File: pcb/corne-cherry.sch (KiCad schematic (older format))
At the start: 142 parts, among them J1 MJ-4PP-9, J2 OLED, J3 MJ-4PP-9, J4 OLED, J5 Conn_01x01_Male, J6 Conn_01x01_Male, P1 Conn_01x03, P3 Conn_01x03, SW1 SW_PUSH, SW10 SW_PUSH, SW11 SW_PUSH, SW12 SW_PUSH, SW13 SW_PUSH, SW14 SW_PUSH, SW15 SW_PUSH, SW16 SW_PUSH, SW17 SW_PUSH, SW18 SW_PUSH, SW19 SW_PUSH, SW2 SW_PUSH, SW20 SW_PUSH, SW21 SW_PUSH, SW22 SW_PUSH, SW23 SW_PUSH, SW24 SW_PUSH, SW25 SW_PUSH, SW26 SW_PUSH, SW27 SW_PUSH, SW28 SW_PUSH, SW29 SW_PUSH, SW3 SW_PUSH, SW30 SW_PUSH, SW31 SW_PUSH, SW32 SW_PUSH, SW33 SW_PUSH, SW34 SW_PUSH, SW35 SW_PUSH, SW36 SW_PUSH, SW37 SW_PUSH, SW38 SW_PUSH, SW39 SW_PUSH, SW4 SW_PUSH, SW40 SW_PUSH, SW41 SW_PUSH, SW42 SW_PUSH, SW5 SW_PUSH, SW6 SW_PUSH, SW7 SW_PUSH, SW8 SW_PUSH, SW9 SW_PUSH, U1 ProMicro, U2 ProMicro

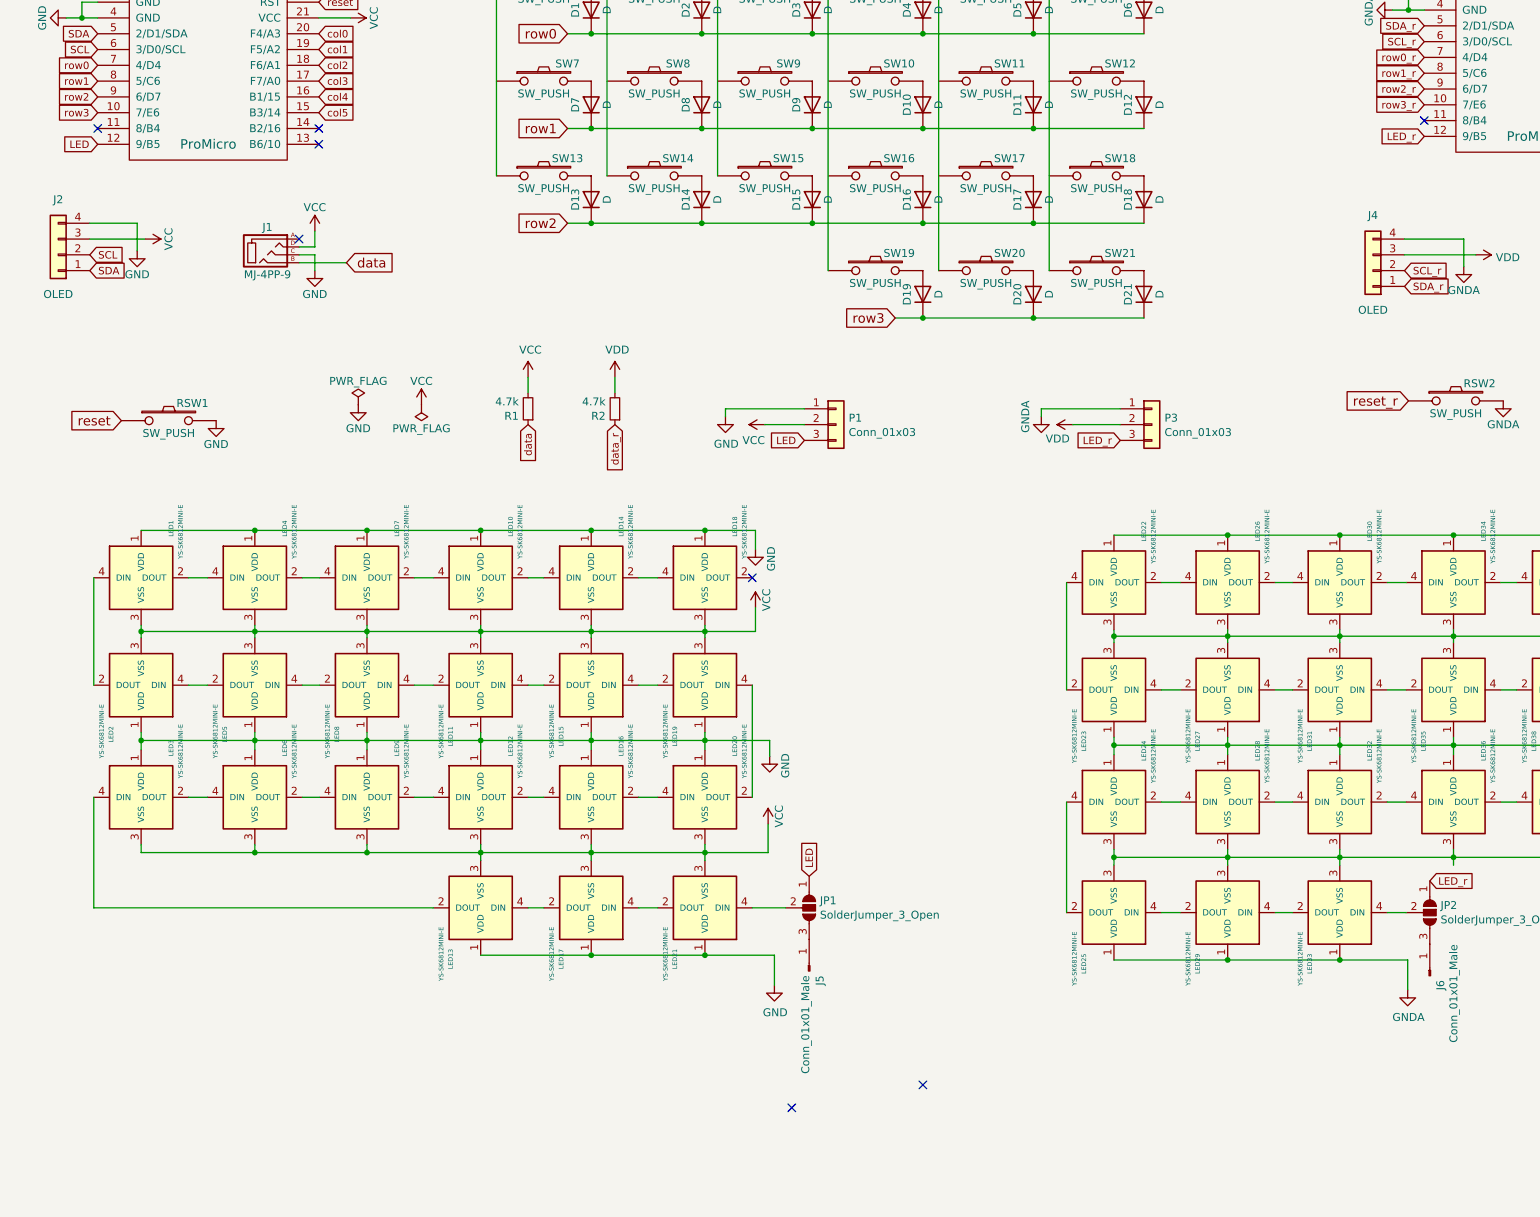
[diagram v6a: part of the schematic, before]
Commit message: Add PCB documentation
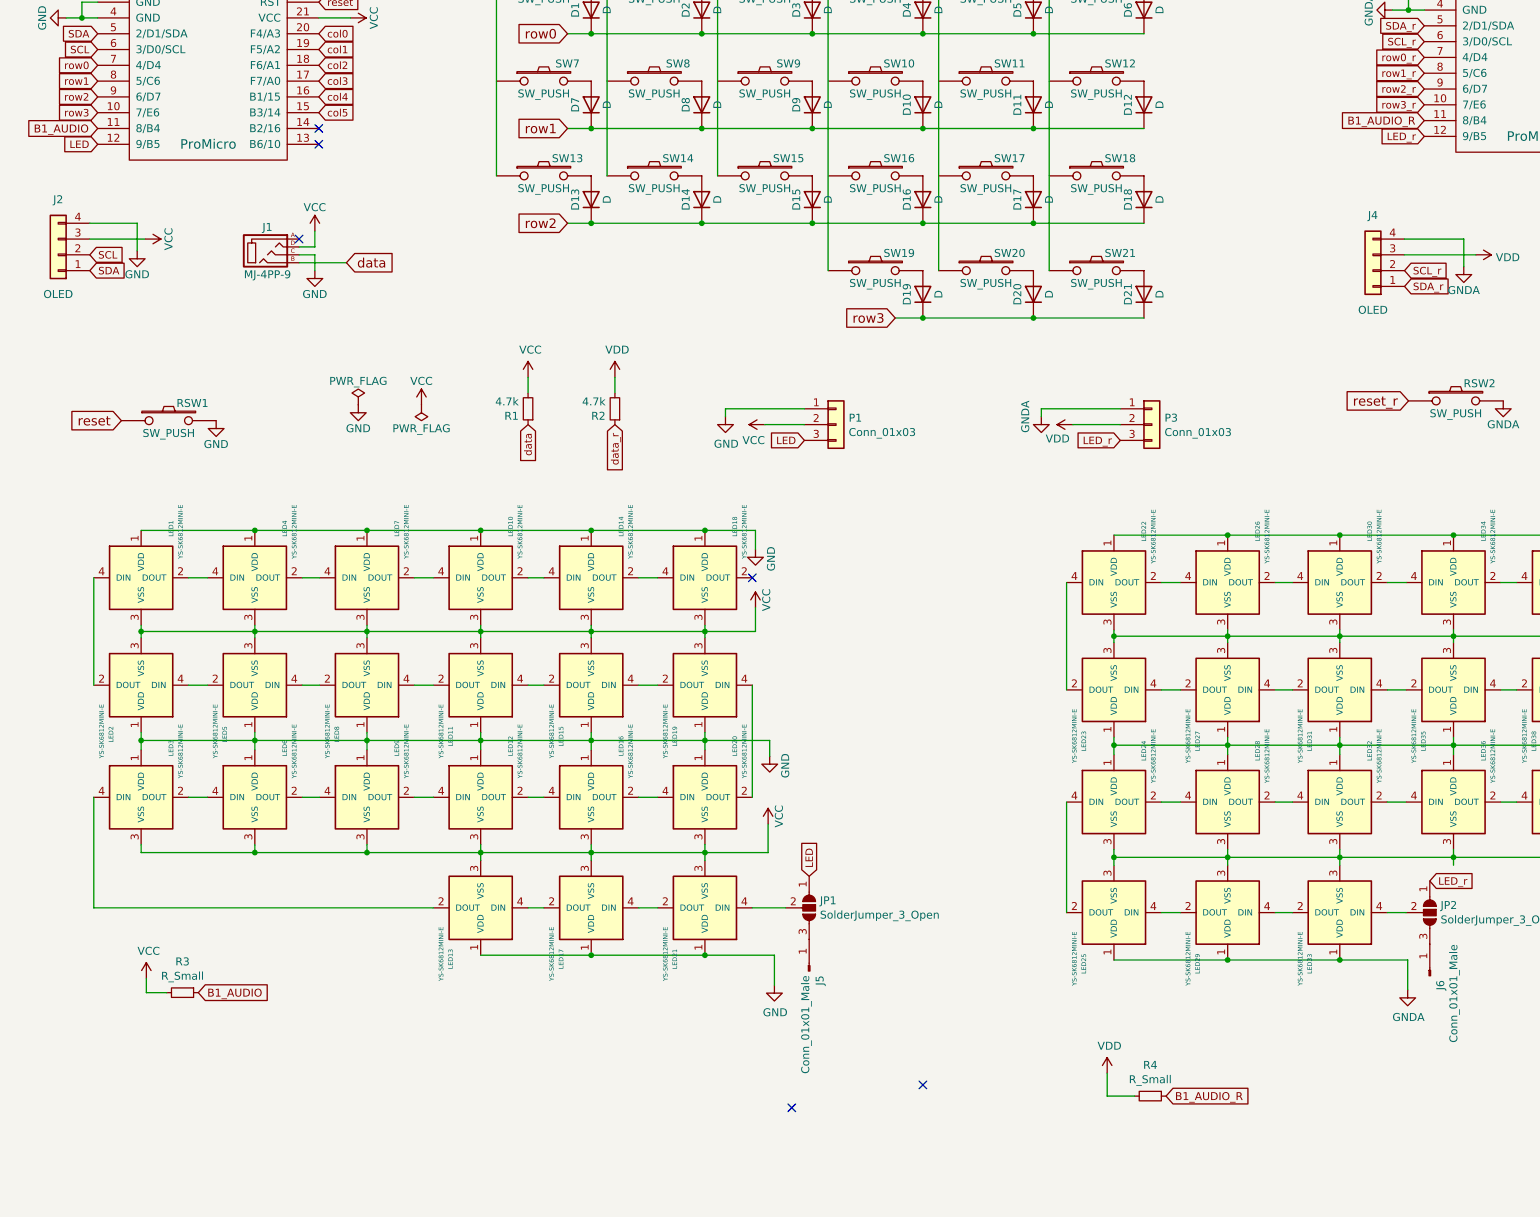
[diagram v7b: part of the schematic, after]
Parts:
- added R3, R4: R_Small, Buzzer_Beeper:Buzzer_Mallory_AST1109MLTRQ, symbol Device:R_Small
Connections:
- net VCC: now also R3.2
- net VDD: now also R4.2
- net B1_AUDIO: now reaches U1.11 (8/B4)
- net B1_AUDIO: now also R3.1
- net B1_AUDIO_R: now reaches U2.11 (8/B4)
- net B1_AUDIO_R: now also R4.1
- no-connect marks 17 -> 15
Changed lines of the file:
@@
 col0
 NoConn ~ 2475 2175
-NoConn ~ 1075 2175
 Text GLabel 1075 1575 0    47   Input ~ 0
 SDA
@@
 col0_r
 NoConn ~ 10875 2125
-NoConn ~ 9475 2125
 Text GLabel 9475 1525 0    47   Input ~ 0
 SDA_r
@@
 	1    0    0    -1
 $EndComp
+$Comp
+L Device:R_Small R3
+U 1 1 6062157F
+P 1612 7647
+F 0 "R3" V 1416 7647 50  0000 C CNN
+F 1 "R_Small" V 1507 7647 50  0000 C CNN
+F 2 "Buzzer_Beeper:Buzzer_Mallory_AST1109MLTRQ" H 1612 7647 50  0001 C CNN
+F 3 "~" H 1612 7647 50  0001 C CNN
+	1    1612 7647
+	0    1    1    0
+$EndComp
+Wire Wire Line
+	1512 7647 1383 7647
+Wire Wire Line
+	1383 7647 1383 7557
+$Comp
+L power:VCC #PWR0117
+U 1 1 606BAF80
+P 1383 7557
+F 0 "#PWR0117" H 1383 7407 50  0001 C CNN
+F 1 "VCC" H 1398 7730 50  0000 C CNN
+F 2 "" H 1383 7557 50  0001 C CNN
+F 3 "" H 1383 7557 50  0001 C CNN
+	1    1383 7557
+	1    0    0    -1
+$EndComp
+$Comp
+L Device:R_Small R4
+U 1 1 606DACBD
+P 7740 8302
+F 0 "R4" V 7544 8302 50  0000 C CNN
+F 1 "R_Small" V 7635 8302 50  0000 C CNN
+F 2 "Buzzer_Beeper:Buzzer_Mallory_AST1109MLTRQ" H 7740 8302 50  0001 C CNN
+F 3 "~" H 7740 8302 50  0001 C CNN
+	1    7740 8302
+	0    1    1    0
+$EndComp
+Text GLabel 7840 8302 2    50   Input ~ 0
+B1_AUDIO_R
+Wire Wire Line
+	7640 8302 7467 8302
+$Comp
+L power:VDD #PWR0118
+U 1 1 606F170B
+P 7467 8158
+F 0 "#PWR0118" H 7467 8008 50  0001 C CNN
+F 1 "VDD" H 7482 8331 50  0000 C CNN
+F 2 "" H 7467 8158 50  0001 C CNN
+F 3 "" H 7467 8158 50  0001 C CNN
+	1    7467 8158
+	1    0    0    -1
+$EndComp
+Wire Wire Line
+	7467 8158 7467 8302
+Text GLabel 9475 2125 0    50   Input ~ 0
+B1_AUDIO_R
+Text GLabel 1712 7647 2    50   Input ~ 0
+B1_AUDIO
+Text GLabel 1075 2175 0    50   Input ~ 0
+B1_AUDIO
 $EndSCHEMATC

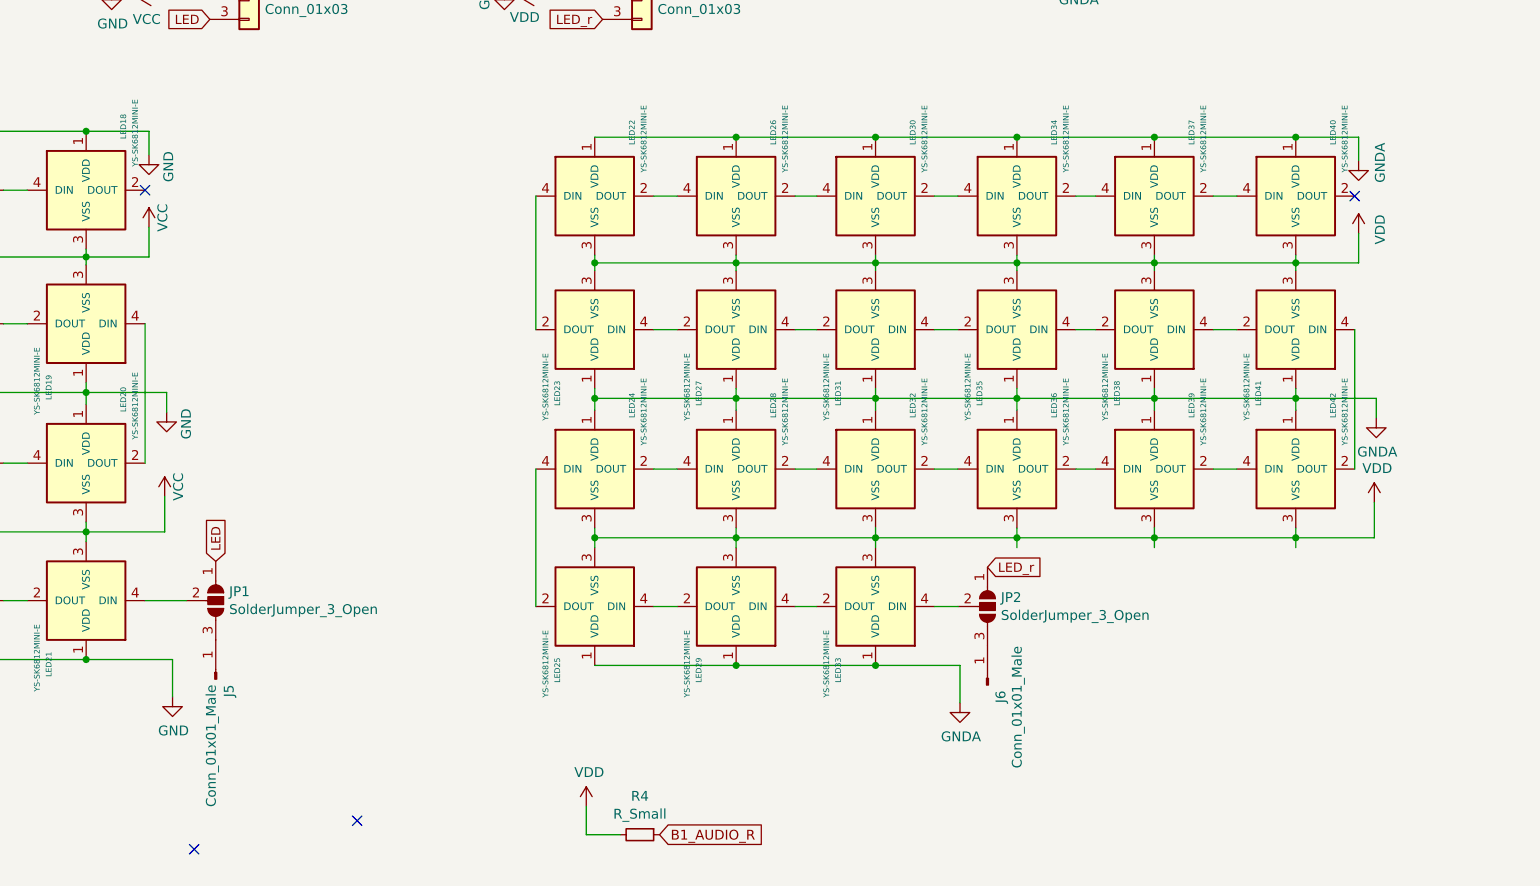
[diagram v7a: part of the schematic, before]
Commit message: Start reworking PCB
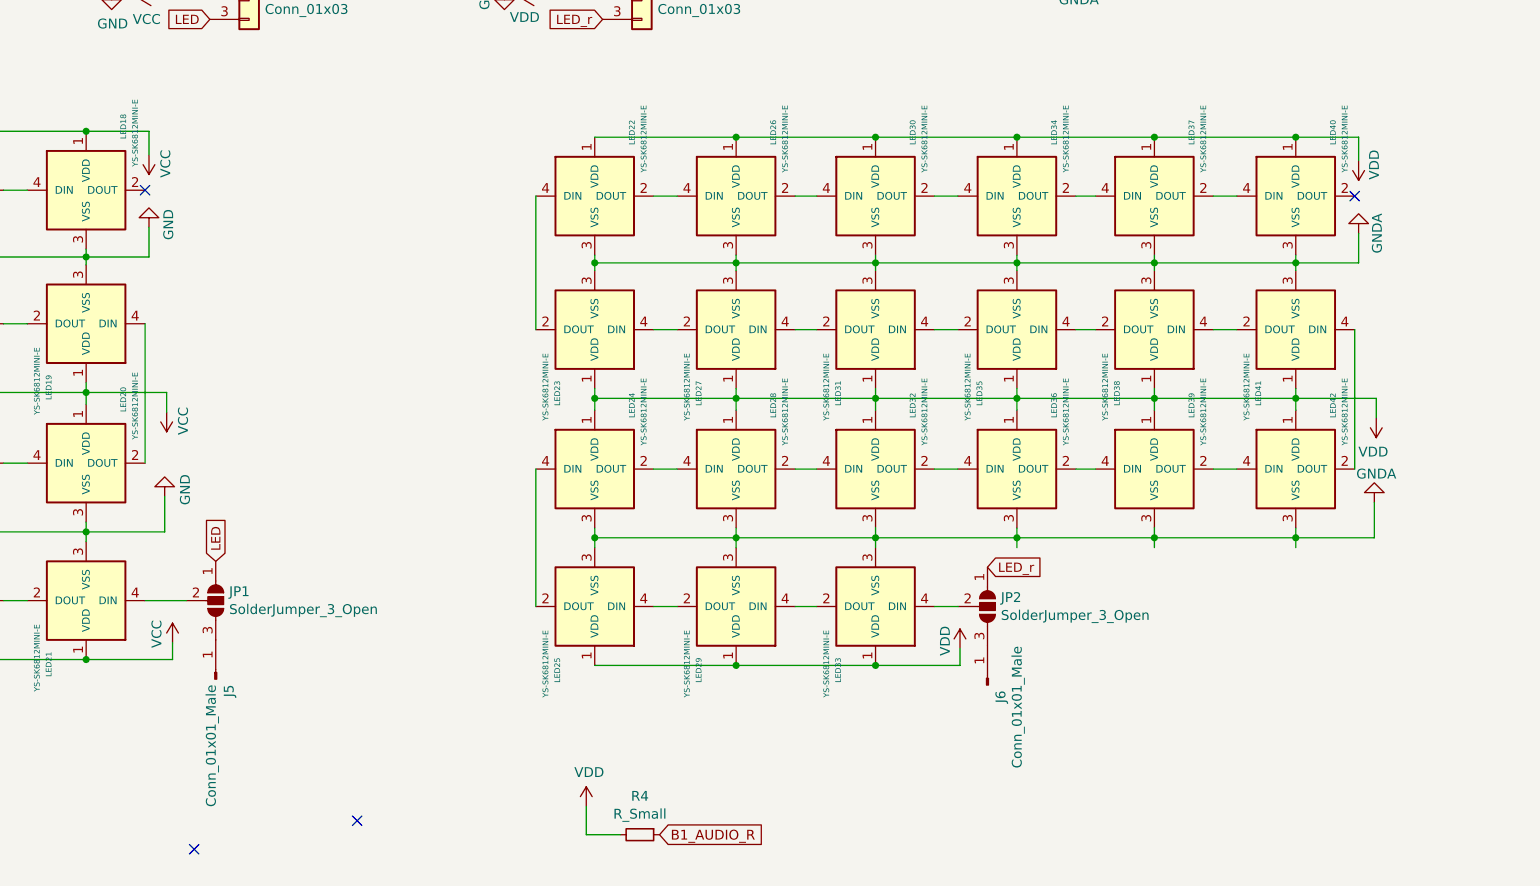
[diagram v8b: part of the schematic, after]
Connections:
- net GND: now also LED1.3 (VSS), LED10.3 (VSS), LED11.3 (VSS), LED12.3 (VSS), LED13.3 (VSS), LED14.3 (VSS), LED15.3 (VSS), LED16.3 (VSS), LED17.3 (VSS), LED18.3 (VSS), LED19.3 (VSS), LED2.3 (VSS), LED20.3 (VSS), LED21.3 (VSS), LED3.3 (VSS), LED4.3 (VSS), LED5.3 (VSS), LED6.3 (VSS), LED7.3 (VSS), LED8.3 (VSS), LED9.3 (VSS); no longer LED1.1 (VDD), LED10.1 (VDD), LED11.1 (VDD), LED12.1 (VDD), LED13.1 (VDD), LED14.1 (VDD), LED15.1 (VDD), LED16.1 (VDD), LED17.1 (VDD), LED18.1 (VDD), LED19.1 (VDD), LED2.1 (VDD), LED20.1 (VDD), LED21.1 (VDD), LED3.1 (VDD), LED4.1 (VDD), LED5.1 (VDD), LED6.1 (VDD), LED7.1 (VDD), LED8.1 (VDD), LED9.1 (VDD)
- net GNDA: now also LED22.3 (VSS), LED23.3 (VSS), LED24.3 (VSS), LED25.3 (VSS), LED26.3 (VSS), LED27.3 (VSS), LED28.3 (VSS), LED29.3 (VSS), LED30.3 (VSS), LED31.3 (VSS), LED32.3 (VSS), LED33.3 (VSS), LED34.3 (VSS), LED35.3 (VSS), LED36.3 (VSS), LED37.3 (VSS), LED38.3 (VSS), LED39.3 (VSS), LED40.3 (VSS), LED41.3 (VSS), LED42.3 (VSS); no longer LED22.1 (VDD), LED23.1 (VDD), LED24.1 (VDD), LED25.1 (VDD), LED26.1 (VDD), LED27.1 (VDD), LED28.1 (VDD), LED29.1 (VDD), LED30.1 (VDD), LED31.1 (VDD), LED32.1 (VDD), LED33.1 (VDD), LED34.1 (VDD), LED35.1 (VDD), LED36.1 (VDD), LED37.1 (VDD), LED38.1 (VDD), LED39.1 (VDD), LED40.1 (VDD), LED41.1 (VDD), LED42.1 (VDD)
- net VCC: now also LED1.1 (VDD), LED10.1 (VDD), LED11.1 (VDD), LED12.1 (VDD), LED13.1 (VDD), LED14.1 (VDD), LED15.1 (VDD), LED16.1 (VDD), LED17.1 (VDD), LED18.1 (VDD), LED19.1 (VDD), LED2.1 (VDD), LED20.1 (VDD), LED21.1 (VDD), LED3.1 (VDD), LED4.1 (VDD), LED5.1 (VDD), LED6.1 (VDD), LED7.1 (VDD), LED8.1 (VDD), LED9.1 (VDD); no longer LED1.3 (VSS), LED10.3 (VSS), LED11.3 (VSS), LED12.3 (VSS), LED13.3 (VSS), LED14.3 (VSS), LED15.3 (VSS), LED16.3 (VSS), LED17.3 (VSS), LED18.3 (VSS), LED19.3 (VSS), LED2.3 (VSS), LED20.3 (VSS), LED21.3 (VSS), LED3.3 (VSS), LED4.3 (VSS), LED5.3 (VSS), LED6.3 (VSS), LED7.3 (VSS), LED8.3 (VSS), LED9.3 (VSS)
- net VDD: now also LED22.1 (VDD), LED23.1 (VDD), LED24.1 (VDD), LED25.1 (VDD), LED26.1 (VDD), LED27.1 (VDD), LED28.1 (VDD), LED29.1 (VDD), LED30.1 (VDD), LED31.1 (VDD), LED32.1 (VDD), LED33.1 (VDD), LED34.1 (VDD), LED35.1 (VDD), LED36.1 (VDD), LED37.1 (VDD), LED38.1 (VDD), LED39.1 (VDD), LED40.1 (VDD), LED41.1 (VDD), LED42.1 (VDD); no longer LED22.3 (VSS), LED23.3 (VSS), LED24.3 (VSS), LED25.3 (VSS), LED26.3 (VSS), LED27.3 (VSS), LED28.3 (VSS), LED29.3 (VSS), LED30.3 (VSS), LED31.3 (VSS), LED32.3 (VSS), LED33.3 (VSS), LED34.3 (VSS), LED35.3 (VSS), LED36.3 (VSS), LED37.3 (VSS), LED38.3 (VSS), LED39.3 (VSS), LED40.3 (VSS), LED41.3 (VSS), LED42.3 (VSS)
